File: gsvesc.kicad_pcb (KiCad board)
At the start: 4 copper layers, 111 x 111 mm, 125 parts, among them J1 Conn_01x06, J10 PHASE_C, J11 PHASE_A, J12 NTC, J13 PHASE_B, J14 Conn_02x04_Odd_Even, J2 Conn_01x06, J3 Conn_01x06, J4 Conn_01x05, J5 Conn_01x03, J6 USB_B_Mini, J7 BAT+, J8 BAT-, Q1 NVMFS5C604, Q2 NVMFS5C604, Q3 NVMFS5C604, Q4 NVMFS5C604, Q5 NVMFS5C604, Q6 NVMFS5C604, U1 STM32F405RGTx, U2 IRU1010-33, U3 DRV8301DCAR, U4 AD8418, U5 AD8418, U6 AD8418, U7 M74VHC1GT66DTT1G, U8 M74VHC1GT66DTT1G, U9 M74VHC1GT66DTT1G, Y1 ABM3B 8MHz

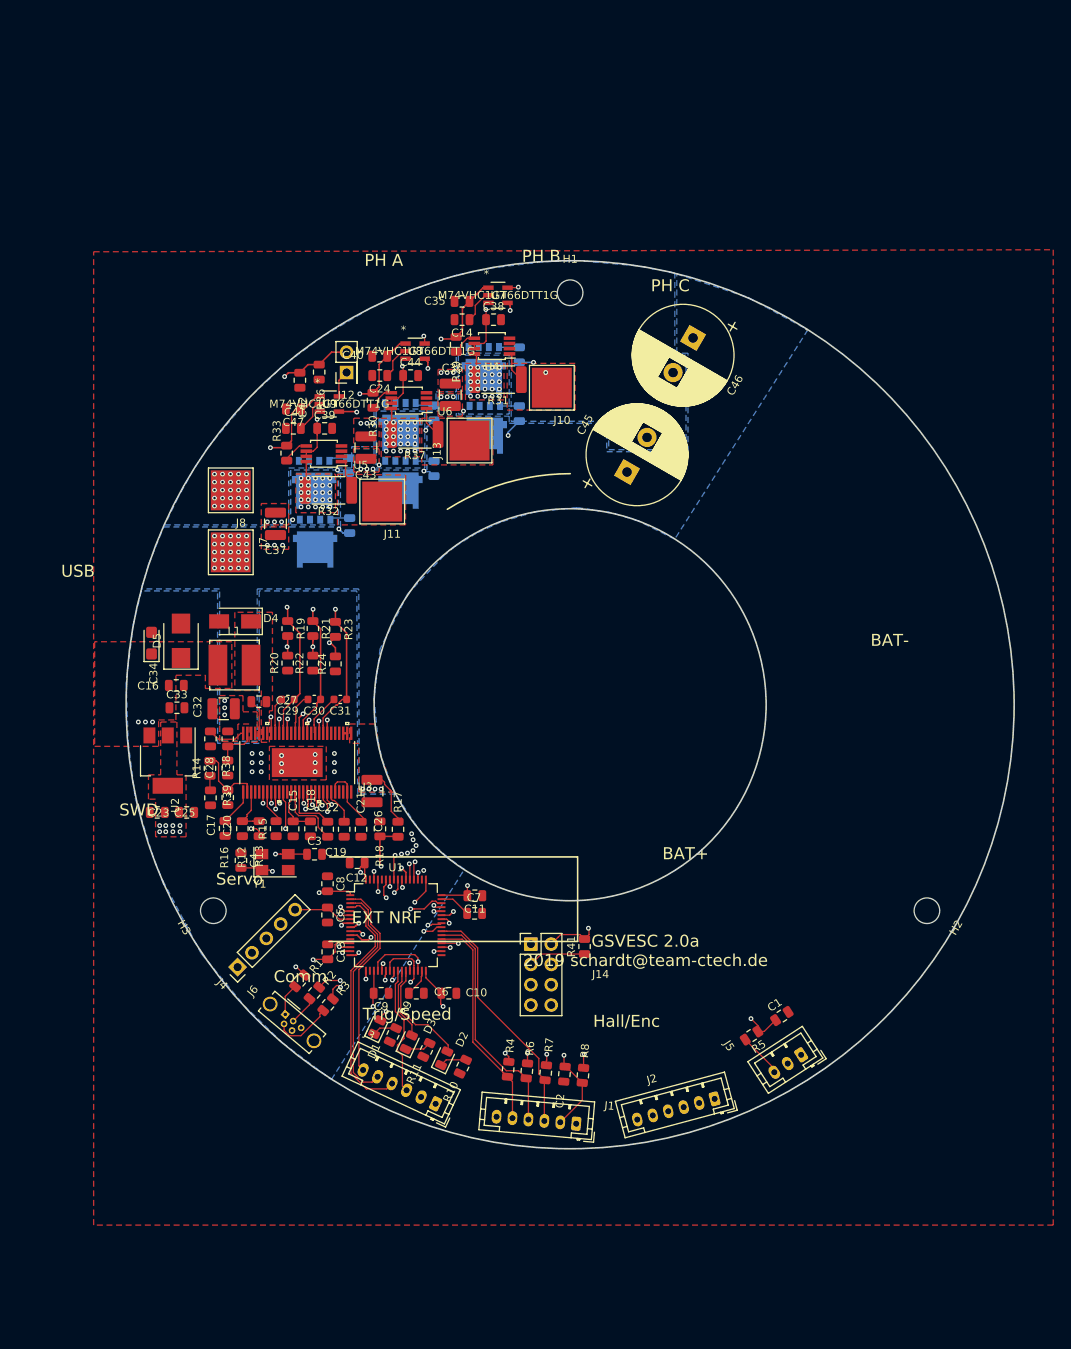
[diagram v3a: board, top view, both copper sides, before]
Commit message: First Version V3 - Change FET to TPH2R506PL - 1oz copper on all layer - switch analog amp to INA240 - remove Elkos - add more ceramic c - separate current measurement tracks from gate driver tracks - vbat now 36V
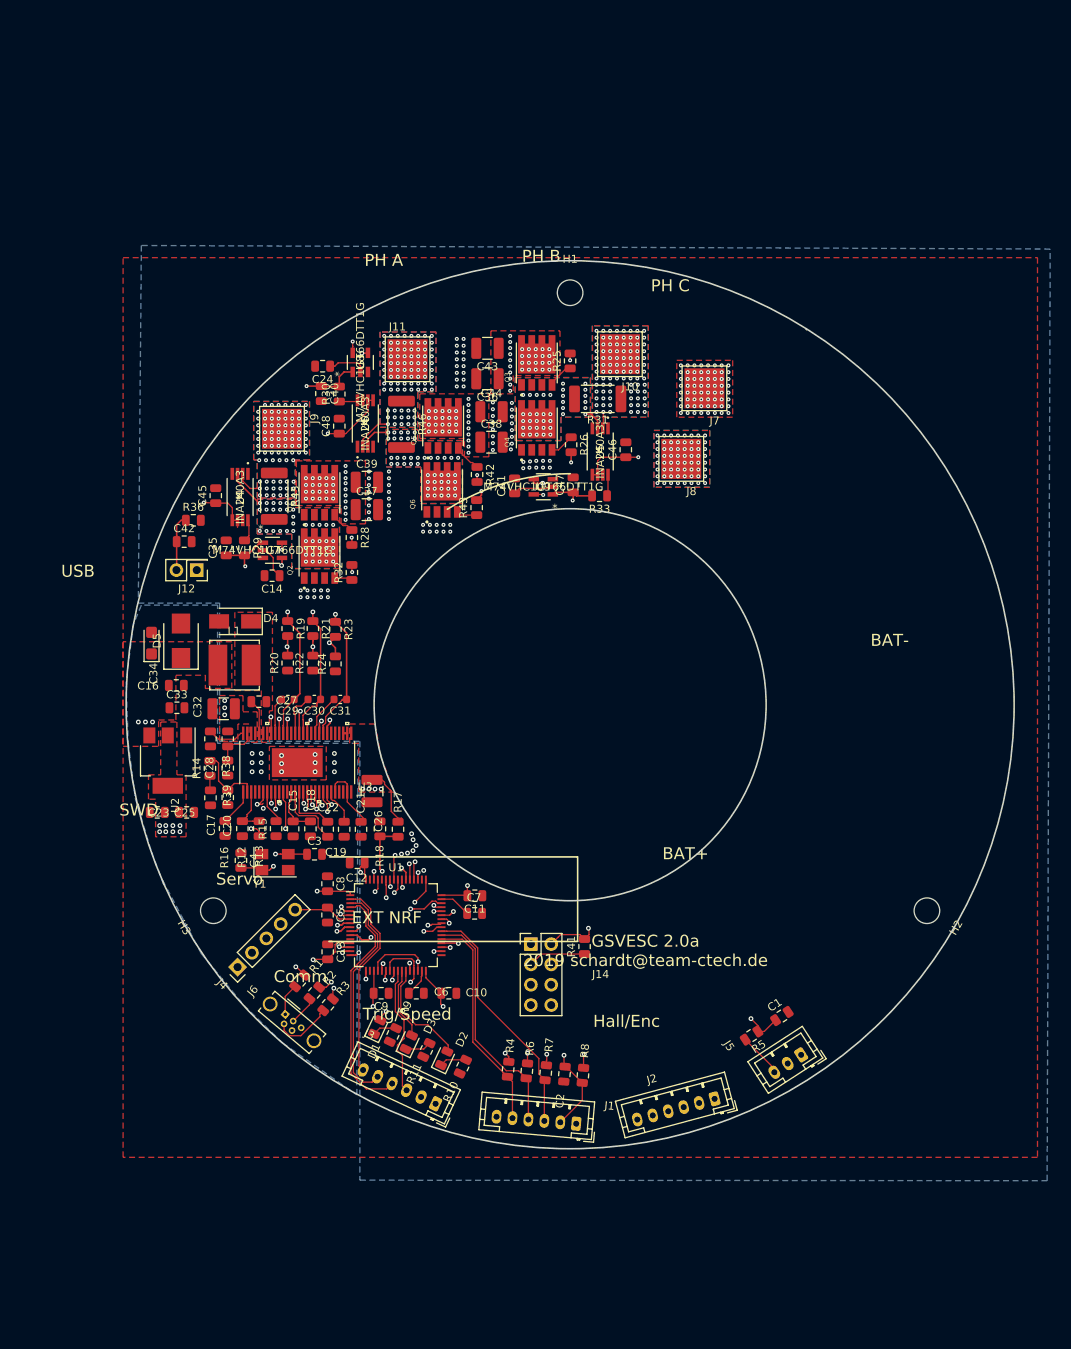
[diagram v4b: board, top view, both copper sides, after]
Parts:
- removed J13: PHASE_B, gsvesc:TestPoint_Pad_5.0x5.0mm
- removed R27, R34, R35: 4R75, Resistor_SMD:R_0805_2012Metric
- removed R37: 0R0005, Resistor_SMD:R_2512_6332Metric
- added C48: 100n, Capacitor_SMD:C_0805_2012Metric, F.Cu at (71.1, 65.2)
- added J9: PHASE_A, gsvesc:TestPoint_Pad_5.0x5.0mm, F.Cu at (64.0, 65.5)
- added R42: 4R75, Resistor_SMD:R_0805_2012Metric, F.Cu at (88.4, 71.2)
- added R43: 4R75, Resistor_SMD:R_0805_2012Metric, F.Cu at (88.3, 75.4)
- added R45: 0R0005, Resistor_SMD:R_2512_6332Metric, F.Cu at (63.0, 73.9)
- added R46: 0R0005, Resistor_SMD:R_2512_6332Metric, F.Cu at (78.9, 64.9)
- C26, C32, C36, C37, C43: value 10u0/100V -> 10u0/75V
- C38, C39, C44: value 10u0/16V -> 10u0/75V; footprint Capacitor_SMD:C_0805_2012Metric -> Capacitor_SMD:C_1210_3225Metric
- C45, C46: value 680u/63V -> 100n; footprint Capacitor_THT:CP_Radial_D12.5mm_P5.00mm -> Capacitor_SMD:C_0805_2012Metric
- J11: value PHASE_A -> PHASE_B
- Q1, Q2, Q3, Q4, Q5, Q6: value NVMFS5C604 -> TPH2R506PL; footprint gsvesc:DFN500X600X110-5N -> gsvesc:TRANS_TPHR8504PL-3PIN; moved to F.Cu
- R25, R26, R28: moved to F.Cu
- R32: value 0R0005 -> 4R75; footprint Resistor_SMD:R_2512_6332Metric -> Resistor_SMD:R_0805_2012Metric
- U4, U5, U6: value AD8418 -> INA240A3; footprint Package_SO:MSOP-8_3x3mm_P0.65mm -> gsvesc:INA240A1QPWRQ1
- moved J7 62.7 mm to (116.8, 60.5), turned to 180 degrees
- moved J8 56.4 mm to (113.9, 69.3)
- moved C45 51.5 mm to (55.7, 73.9), turned to 90 degrees
- moved C35 42.6 mm to (57.0, 80.4), turned to 90 degrees
- moved U7 42.6 mm to (62.8, 80.7)
- moved C14 39.9 mm to (62.7, 83.9)
- moved R33 39.5 mm to (103.7, 73.9), turned to 180 degrees
- moved U4 36.7 mm to (58.8, 74.0), turned to 270 degrees
- moved R29 36.7 mm to (59.3, 80.4), turned to 270 degrees
- moved C47 36.2 mm to (100.4, 72.5), turned to 90 degrees
- moved Q3 35.6 mm to (95.8, 57.3), turned to 90 degrees
- moved U5 34.5 mm to (103.8, 68.4), turned to 270 degrees
- moved Q2 31.1 mm to (68.7, 81.4), turned to 90 degrees
- moved J12 31.0 mm to (53.3, 83.2), turned to 180 degrees
- moved Q4 28.7 mm to (95.8, 65.4), turned to 90 degrees
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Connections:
- C35 pad 1: /MCU/CURRENT_3 -> /MCU/CURRENT_1
- C38 pad 1: VCC -> /DRV8301/VBAT
- C39 pad 1: VCC -> /DRV8301/VBAT
- C44 pad 1: VCC -> /DRV8301/VBAT
- C45 pad 1: /DRV8301/VBAT -> VCC
- C46 pad 1: /DRV8301/VBAT -> VCC
- C47 pad 1: /MCU/CURRENT_1 -> /MCU/CURRENT_3
- J11 pad 1: /POWER/PHASE_A -> /POWER/PHASE_B
- Q1 pad 3: /DRV8301/SH_C -> /DRV8301/SH_A
- Q2 pad 1: /DRV8301/SH_C -> /DRV8301/SH_A
- Q3 pad 3: /DRV8301/SH_A -> /DRV8301/SH_C
- Q4 pad 1: /DRV8301/SH_A -> /DRV8301/SH_C
- R25 pad 1: Net-(Q1-Pad2) -> Net-(Q3-Pad2)
- R26 pad 1: Net-(Q2-Pad2) -> Net-(Q4-Pad2)
- R28 pad 1: Net-(Q4-Pad2) -> Net-(Q1-Pad2)
- R28 pad 2: /DRV8301/GL_A -> /DRV8301/GH_A
- R29 pad 1: /POWER/C_C -> /POWER/C_A
- R29 pad 2: /MCU/CURRENT_3 -> /MCU/CURRENT_1
- R32 pad 1: /POWER/PHASE_A -> Net-(Q2-Pad2)
- R32 pad 2: /DRV8301/SH_A -> /DRV8301/GL_A
- R33 pad 1: /POWER/C_A -> /POWER/C_C
- R33 pad 2: /MCU/CURRENT_1 -> /MCU/CURRENT_3
- U4 pad 1: /POWER/PHASE_C -> (no net)
- U4 pad 2: GND -> /POWER/PHASE_A
- U4 pad 3: GND -> /DRV8301/SH_A
- U4 pad 4: Net-(U4-Pad4) -> GND
- U4 pad 5: /POWER/C_C -> VCC
- U4 pad 7: VCC -> GND
- U4 pad 8: /DRV8301/SH_C -> /POWER/C_A
- U5 pad 1: /POWER/PHASE_A -> (no net)
- U5 pad 2: GND -> /POWER/PHASE_C
- U5 pad 3: GND -> /DRV8301/SH_C
- U5 pad 4: Net-(U5-Pad4) -> GND
- U5 pad 5: /POWER/C_A -> VCC
- U5 pad 7: VCC -> GND
- U5 pad 8: /DRV8301/SH_A -> /POWER/C_C
- U6 pad 1: /POWER/PHASE_B -> (no net)
- U6 pad 2: GND -> /POWER/PHASE_B
- U6 pad 3: GND -> /DRV8301/SH_B
- U6 pad 4: Net-(U6-Pad4) -> GND
- U6 pad 5: /POWER/C_B -> VCC
- U6 pad 7: VCC -> GND
- U6 pad 8: /DRV8301/SH_B -> /POWER/C_B
- U7 pad 1: /MCU/CURRENT_3 -> /MCU/CURRENT_1
- U9 pad 1: /MCU/CURRENT_1 -> /MCU/CURRENT_3
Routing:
- net /POWER/CURR_FILTER: track 91.1 -> 158.9 mm, vias 4 -> 5
- net /MCU/ADC_TEMP: track 93.4 -> 77.9 mm, vias 2 -> 1
- net /MCU/CURRENT_1: track 75.8 -> 60.3 mm
- net /DRV8301/GH_C: track 50.0 -> 65.1 mm
- net /MCU/CURRENT_2: track 78.8 -> 90.1 mm
- net /DRV8301/GL_A: track 37.9 -> 28.0 mm
- net /MCU/CURRENT_3: track 93.2 -> 101.0 mm
- net /DRV8301/GH_B: track 40.8 -> 45.2 mm
- net /DRV8301/GL_C: track 58.8 -> 54.6 mm
- net /DRV8301/SH_C: track 50.9 -> 55.0 mm, vias 27 -> 38
- net /DRV8301/SH_A: track 32.2 -> 28.8 mm, vias 27 -> 46
- net VCC: track 67.5 -> 70.8 mm, vias 26 -> 27
- net /DRV8301/GL_B: track 46.1 -> 43.7 mm
- net /POWER/PHASE_C: track 3.77 -> 2.07 mm, vias 1 -> 94
- net /DRV8301/GH_A: track 30.2 -> 31.6 mm
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- added copper zone on B.Cu, net /POWER/PHASE_A
- added copper zone on In1.Cu, net /POWER/PHASE_A
- added copper zone on In2.Cu, net /POWER/PHASE_A
- added copper zone on B.Cu, net /POWER/PHASE_B
- added copper zone on In1.Cu, net /POWER/PHASE_B
- added copper zone on In2.Cu, net /POWER/PHASE_B
- added copper zone on B.Cu, net /POWER/PHASE_C
- added copper zone on In1.Cu, net /POWER/PHASE_C
- added copper zone on In2.Cu, net /POWER/PHASE_C
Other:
- rule trace_min: 0.15 -> 0.1
- rule via_min_drill: 0.3 -> 0.2
- rule via_min_size: 0.6 -> 0.45

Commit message: Version 3 update - JST as SMD part - move FET tracks
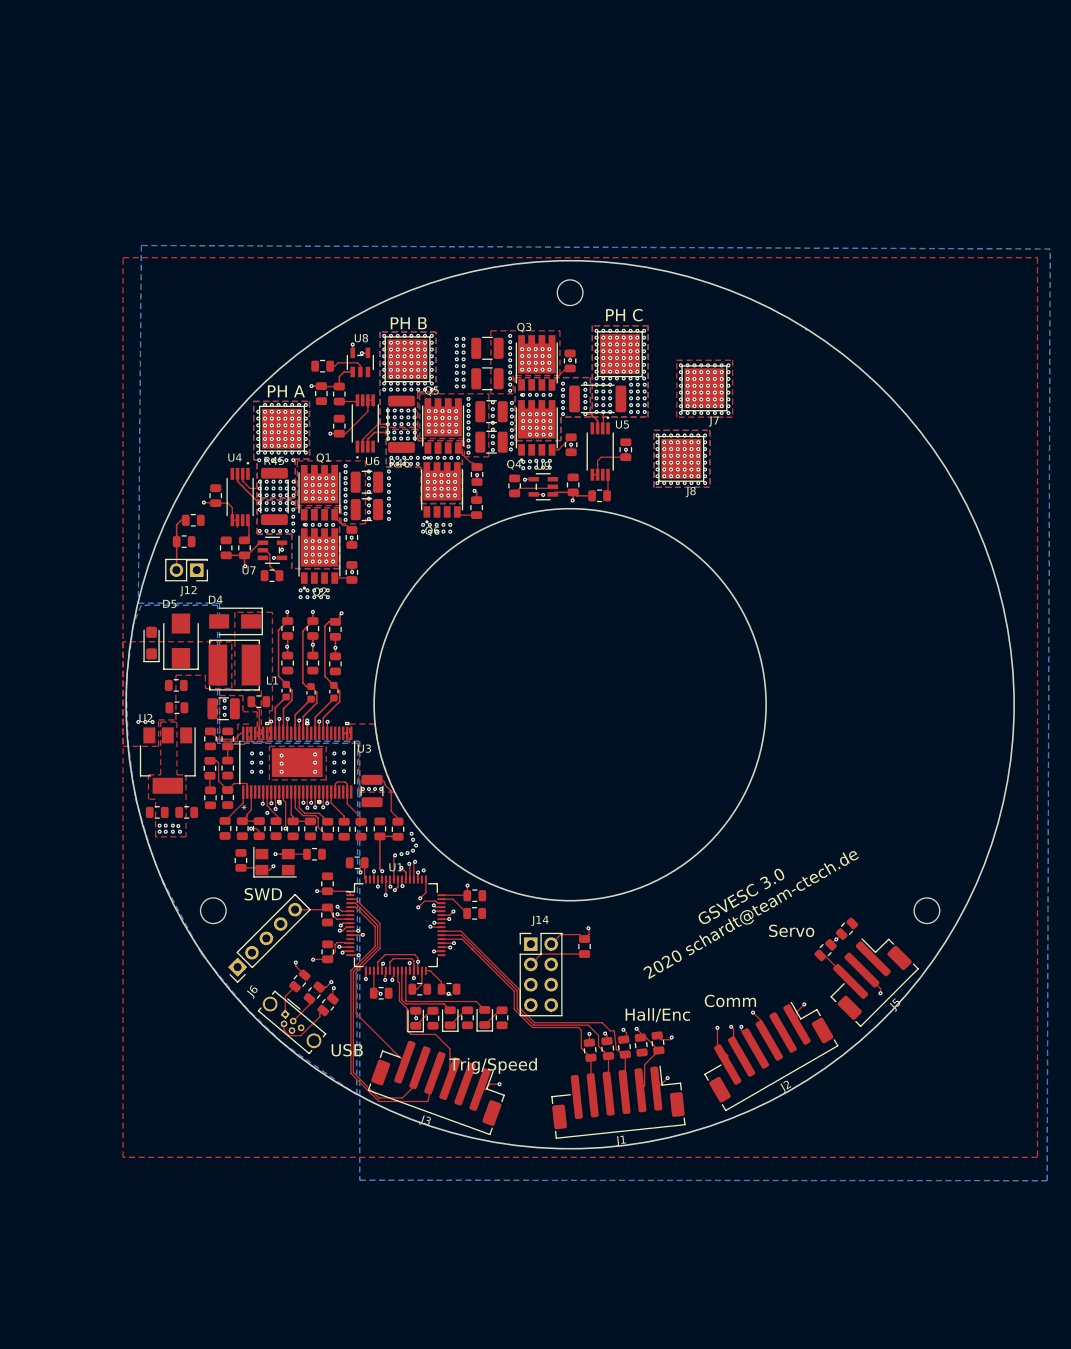
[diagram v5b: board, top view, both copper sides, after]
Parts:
- J1, J2, J3: footprint Connector_JST:JST_PH_B6B-PH-K_1x06_P2.00mm_Vertical -> Connector_JST:JST_PH_B6B-PH-SM4-TB_1x06-1MP_P2.00mm_Vertical
- J5: footprint Connector_JST:JST_PH_B3B-PH-K_1x03_P2.00mm_Vertical -> Connector_JST:JST_PH_B3B-PH-SM4-TB_1x03-1MP_P2.00mm_Vertical
- moved R5 14.1 mm to (131.9, 130.7), turned to 225 degrees
- moved C1 13.6 mm to (134.6, 128.0), turned to 45 degrees
- moved J5 13.0 mm to (136.8, 133.5), turned to 225 degrees
- moved R4 10.5 mm to (102.5, 143.2), turned to 276 degrees
- moved R6 10.5 mm to (104.7, 143.0), turned to 276 degrees
- moved R7 10.3 mm to (106.8, 142.8), turned to 276 degrees
- moved C2 10.3 mm to (108.9, 142.5), turned to 276 degrees
- moved R8 10.2 mm to (111.0, 142.3), turned to 276 degrees
- moved J2 8.89 mm to (124.3, 142.9), turned to 210 degrees
- moved R10 7.83 mm to (91.5, 139.1), turned to 90 degrees
- moved D2 7.20 mm to (89.3, 139.1), turned to 90 degrees
- moved R11 6.52 mm to (87.2, 139.1), turned to 90 degrees
- moved J1 6.11 mm to (105.9, 149.0), turned to 186 degrees
- moved D3 6.02 mm to (85.0, 139.1), turned to 90 degrees
- moved R9 5.42 mm to (82.9, 139.2), turned to 90 degrees
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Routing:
- net /MCU/MISO_ADC_EXT2: track 42.4 -> 52.1 mm, vias 1 -> 2
- net /MCU/TX_SCL_MOSI: track 43.1 -> 52.5 mm, vias 1 -> 2
- net /MCU/RX_SDA_NSS: track 49.0 -> 58.1 mm, vias 1 -> 2
- net VCC: track 70.8 -> 79.4 mm, vias 27 -> 31
- net /MCU/SCK_ADC_EXT: track 44.3 -> 52.8 mm, vias 1 -> 2
- net /MCU/HALL_ROT_B: track 30.5 -> 38.4 mm
- net /MCU/HALL_ROT_A: track 28.5 -> 36.1 mm
- net /MCU/TEMP_MOTOR: track 37.1 -> 44.8 mm
- net /MCU/HALL_3: track 30.5 -> 36.4 mm
- net /DRV8301/SENS_C: track 48.4 -> 43.1 mm
- net /MCU/HALL_1: track 27.6 -> 32.4 mm
- net /POWER/CURR_FILTER: track 158.9 -> 154.6 mm
- net /MCU/HALL_2: track 29.9 -> 33.9 mm
- net /MCU/SERVO: track 61.3 -> 63.6 mm
- net /DRV8301/CS: track 35.4 -> 33.4 mm
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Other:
- net class Default: via_dia 0.6 -> 0.5; via_drill 0.3 -> 0.2
- net class POWER: via_dia 0.6 -> 0.5; via_drill 0.3 -> 0.2
- net class USB: via_dia 0.6 -> 0.5; via_drill 0.3 -> 0.2
- board text added: "GSVESC 3.0 2020 schardt@team-ctech.de"
- board text removed: "BAT+"
- board text removed: "BAT-"
- board text removed: "EXT NRF"
- board text removed: "GSVESC 2.0a 2019 schardt@team-ctech.de"

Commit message: implement remarks/changes from Alex
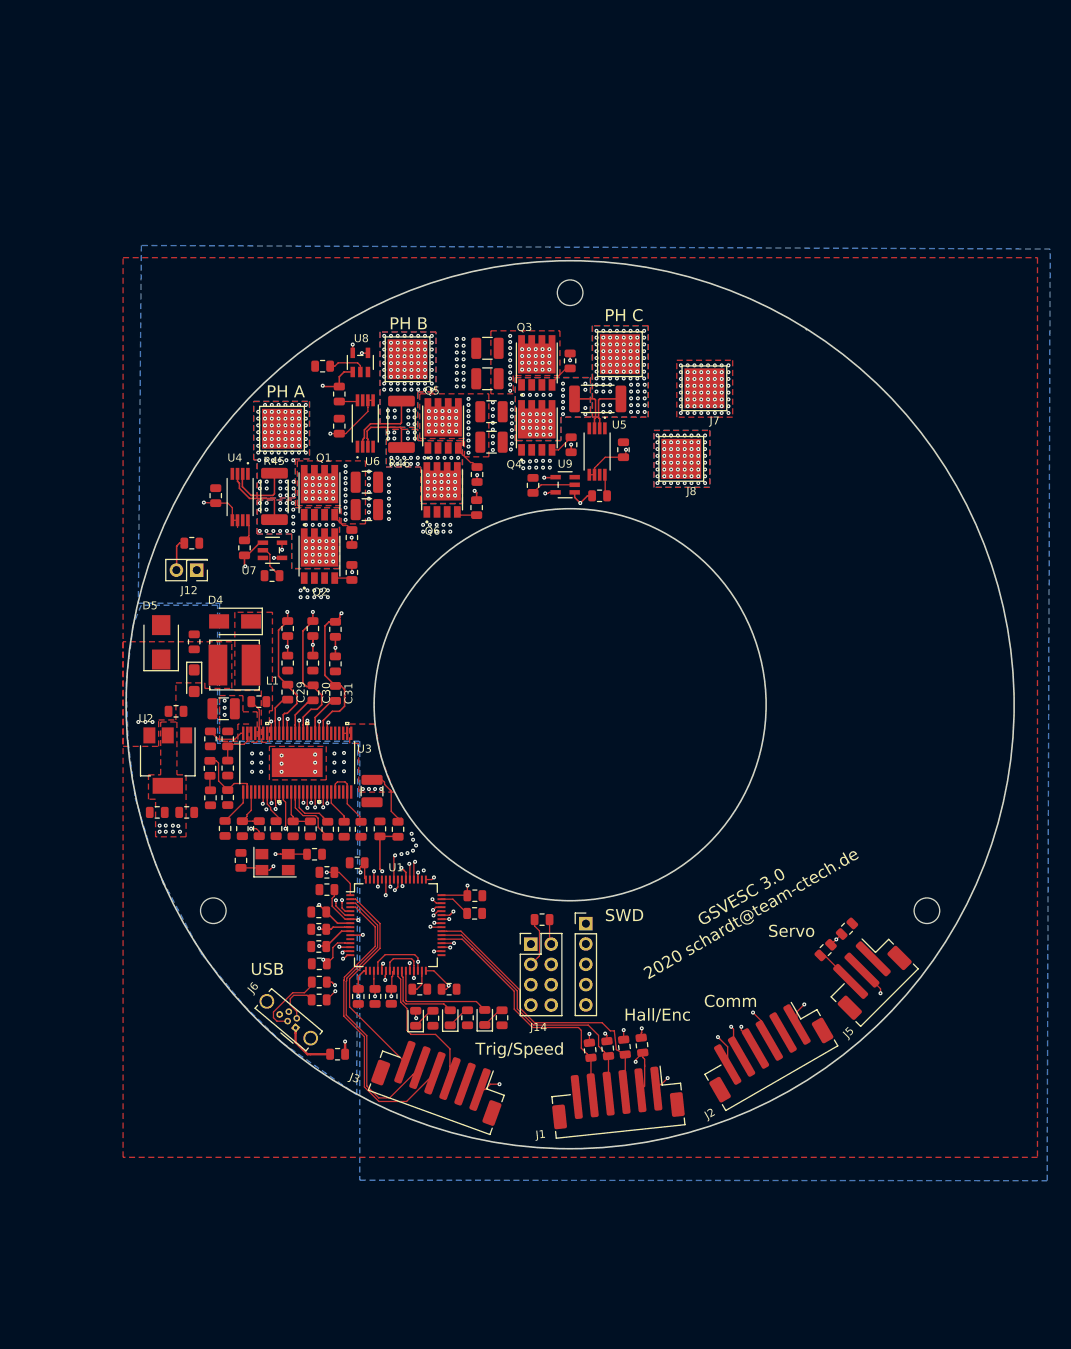
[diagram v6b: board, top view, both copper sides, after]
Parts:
- C29, C30, C31: footprint Capacitor_SMD:C_0603_1608Metric -> Capacitor_SMD:C_0805_2012Metric
- moved C40 67.0 mm to (68.6, 128.1), turned to 180 degrees
- moved C47 65.9 mm to (68.6, 130.2), turned to 180 degrees
- moved C42 60.9 mm to (73.5, 136.5), turned to 270 degrees
- moved C35 47.0 mm to (68.6, 125.9), turned to 180 degrees
- moved J4 43.9 mm to (102.0, 127.4), turned to 0 degrees
- moved C2 31.8 mm to (77.6, 136.4), turned to 270 degrees
- moved R1 10.3 mm to (70.9, 143.7), turned to 180 degrees
- moved C33 8.52 mm to (53.0, 92.1), turned to 90 degrees
- moved C34 7.11 mm to (53.0, 97.0), turned to 270 degrees
- moved R41 6.29 mm to (96.5, 126.9), turned to 0 degrees
- moved C16 3.24 mm to (50.7, 100.8)
- moved C5 3.17 mm to (69.6, 123.1), turned to 180 degrees
- moved R36 2.86 mm to (52.7, 79.8)
- moved U9 2.74 mm to (99.4, 72.5)
- moved D5 2.48 mm to (48.9, 92.2)
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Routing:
- net /MCU/NRST: track 7.79 -> 46.0 mm, vias 0 -> 1
- net /DRV8301/SH_B: track 43.5 -> 49.7 mm, vias 47 -> 45
- net Net-(J6-Pad3): track 3.65 -> 9.25 mm
- net /MCU/SWCLK: track 29.1 -> 23.6 mm
- net VCC: track 79.4 -> 73.9 mm, vias 31 -> 30
- net /POWER/PHASE_A: track 3.43 -> 8.75 mm, vias 87 -> 82
- net /DRV8301/SH_A: track 28.9 -> 34.2 mm, vias 46 -> 44
- net /POWER/PHASE_B: track 4.85 -> 9.90 mm, vias 87 -> 82
- net /MCU/ADC_TEMP: track 77.9 -> 72.9 mm
- net /MCU/SWDIO: track 26.2 -> 31.2 mm
- net /DRV8301/SH_C: track 56.8 -> 61.7 mm, vias 37 -> 35
- net /POWER/PHASE_C: track 2.07 -> 6.46 mm, vias 94 -> 89
- net /MCU/RX_SDA_NSS: track 58.1 -> 61.0 mm
- net /POWER/CURR_FILTER: track 154.6 -> 157.5 mm
- net Net-(J6-Pad1): track 3.98 -> 6.74 mm
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
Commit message: V3 finish, JLC ready
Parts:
- U3: value DRV8301DCAR -> DCA56_6P35X3P61
- U7, U8, U9: value M74VHC1GT66DTT1G -> TSOP-5
